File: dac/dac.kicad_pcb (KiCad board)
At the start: 4 copper layers, 50 x 25 mm, 33 parts, among them J1 USB_B, J2 Conn_01x04_Pin, J3 Conn_01x04_Pin, U1 PCM2902, U2 SPX3819M5-L, Y1 12MHz

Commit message: started layout
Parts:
- moved C3 0.50 mm to (108.7, 89.9)
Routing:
- net /CONN_D+: track 0.00 -> 21.4 mm
- net /CONN_D-: track 0.00 -> 20.6 mm
- net GND: track 0.00 -> 9.49 mm
- net /XTO: track 0.00 -> 9.29 mm
- net /VINL: track 0.00 -> 7.37 mm
- net /XTI: track 0.00 -> 6.44 mm
- net 3V7: track 0.00 -> 6.28 mm
- net VUSB_CONN: track 0.00 -> 3.87 mm
- net VDDI: track 0.00 -> 2.75 mm
- net /VINR: track 0.00 -> 2.74 mm
- net /VCCXI: track 0.00 -> 2.29 mm
- net /VCCP2I: track 0.00 -> 2.13 mm
- net /USB_D+: track 0.00 -> 2.00 mm
- net /USB_D-: track 0.00 -> 1.85 mm
- net /VCOM: track 0.00 -> 0.63 mm, vias 0 -> 1
- added copper zone on F.Cu, net GND
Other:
- board text added: "teardrop here."

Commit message: layout is complete
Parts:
- added TP2: TestPoint, TestPoint:TestPoint_Pad_D1.0mm, F.Cu at (85.8, 94.3)
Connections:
- J2 pad 1: unconnected-(J2-Pin_1-Pad1) -> VBUS
- J2 pad 2: unconnected-(J2-Pin_2-Pad2) -> GND
- J2 pad 3: unconnected-(J2-Pin_3-Pad3) -> /VOUTL
- J2 pad 4: unconnected-(J2-Pin_4-Pad4) -> /VOUTR
- J3 pad 1: unconnected-(J3-Pin_1-Pad1) -> /HID0
- J3 pad 2: unconnected-(J3-Pin_2-Pad2) -> /HID1
- J3 pad 3: unconnected-(J3-Pin_3-Pad3) -> /HID2
- J3 pad 4: unconnected-(J3-Pin_4-Pad4) -> /~{SSPND}
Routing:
- net VBUS: track 0.00 -> 43.4 mm, vias 0 -> 2
- net GND: track 9.49 -> 33.1 mm, vias 0 -> 18
- net CGND: track 0.00 -> 17.7 mm
- net VDDI: track 2.75 -> 19.6 mm
- net /HID2: track 0.00 -> 12.9 mm, vias 0 -> 1
- net /HID1: track 0.00 -> 11.9 mm, vias 0 -> 1
- net /HID0: track 0.00 -> 11.3 mm, vias 0 -> 1
- net /VOUTL: track 0.00 -> 6.56 mm
- net 3V7: track 6.28 -> 0.00 mm
- net /~{SSPND}: track 0.00 -> 5.14 mm
- net /ADJ: track 0.00 -> 4.59 mm
- net /VOUTR: track 0.00 -> 4.36 mm
- net /VCCP1I: track 0.00 -> 3.30 mm, vias 0 -> 1
- net /VCOM: track 0.63 -> 2.12 mm
- net /CONN_D+: track 21.4 -> 22.5 mm
- added copper zone on F.Cu, net 3V7
- added copper zone on In1.Cu, net GND
- added copper zone on In2.Cu, net GND
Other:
- board text removed: "teardrop here."

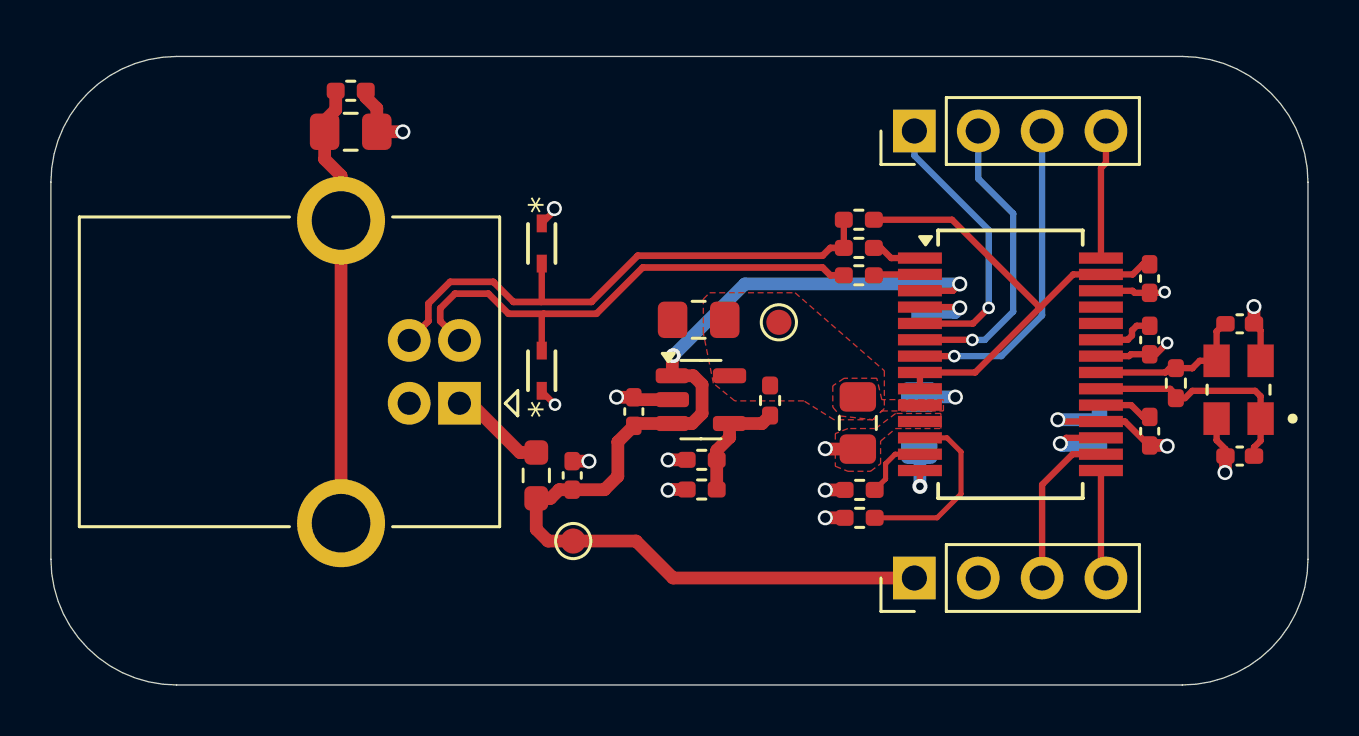
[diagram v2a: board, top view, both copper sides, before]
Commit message: added stitching, redid 3d models
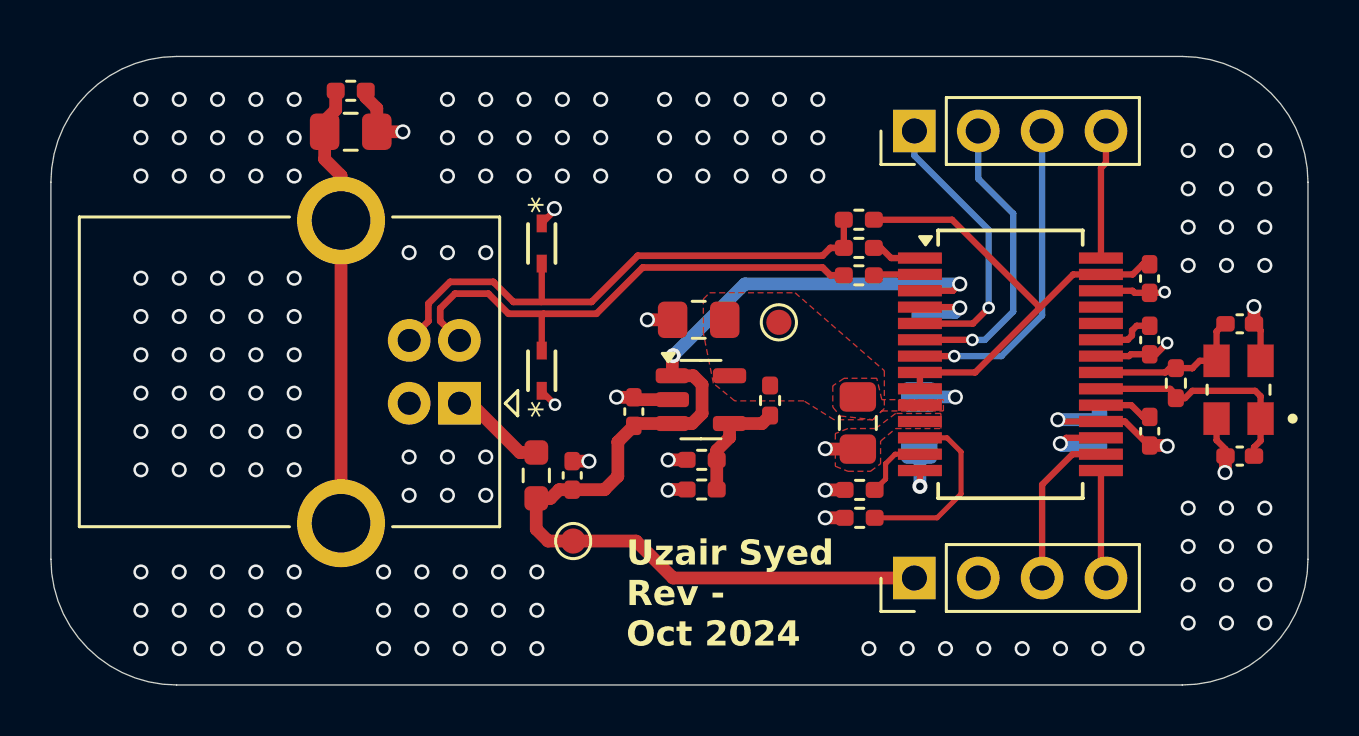
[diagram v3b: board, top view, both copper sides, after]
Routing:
- net GND: track 33.1 -> 34.1 mm, vias 18 -> 165
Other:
- board text added: "Uzair Syed Rev - Oct 2024"

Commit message: added teardrops & extra stitching
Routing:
- net GND: vias 165 -> 170
- added copper zone on F.Cu, net VDDI

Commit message: labeled headers and test points
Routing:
- net GND: vias 170 -> 159
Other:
- board text added: "3V7"
- board text added: "GND"
- board text added: "HID0"
- board text added: "HID1"
- board text added: "HID2"
- board text added: "VBUS"
- board text added: "VL"
- board text added: "VR"
- board text added: "~{SSPND}"

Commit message: final cleanup
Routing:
- net GND: vias 159 -> 161
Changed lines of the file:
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@@
 				(color "White")
 			)
-			(copper_finish "HAL SnPb")
+			(copper_finish "None")
 			(dielectric_constraints yes)
 		)
@@
 	)
 	(gr_text "GND\n"
-		(at 100.6348 98.7044 0)
+		(at 100.7364 98.7044 0)
 		(layer "F.SilkS")
 		(effects
@@
 	)
 	(gr_text "VBUS\n"
-		(at 97.5868 98.806 0)
+		(at 97.4852 98.7044 0)
 		(layer "F.SilkS")
 		(effects
@@
 	)
 	(via
+		(at 103.9876 90.9828)
+		(size 0.6)
+		(drill 0.3)
+		(layers "F.Cu" "B.Cu")
+		(free yes)
+		(net 2)
+	)
+	(via
 		(at 70.104 98.552)
 		(size 0.6)
@@
 	)
 	(via
+		(at 103.886 89.916)
+		(size 0.6)
+		(drill 0.3)
+		(layers "F.Cu" "B.Cu")
+		(free yes)
+		(net 2)
+	)
+	(via
 		(at 68.58 97.028)
 		(size 0.6)
@@
 	)
 	(zone
-		(net 8)
-		(net_name "VBUS")
+		(net 23)
+		(net_name "/VINR")
 		(layer "F.Cu")
 		(name "$teardrop_padvia$")
 		(hatch full 0.1)
-		(priority 30000)
+		(priority 30007)
 		(attr
 			(teardrop
@@
 		(polygon
 			(pts
-				(xy 97.645 95.491) (xy 97.645 95.999) (xy 98.495 96.595) (xy 99.346 95.745) (xy 98.495 94.895)
+				(xy 98.426841 90.829475) (xy 98.570525 90.973159) (xy 98.69 91.045) (xy 99.565707 90.819293) (xy 98.69 90.660946)
 			)
 		)
@@
 	)
 	(zone
-		(net 20)
-		(net_name "/VOUTL")
+		(net 1)
+		(net_name "/VCOM")
 		(layer "F.Cu")
 		(name "$teardrop_padvia$")
 		(hatch full 0.1)
-		(priority 30001)
+		(priority 30008)
 		(attr
 			(teardrop
@@
 		(polygon
 			(pts
-				(xy 104.552 94.045) (xy 104.298 94.045) (xy 103.639702 95.419719) (xy 104.425 95.746) (xy 105.210298 95.419719)
+				(xy 99.438 91.92) (xy 99.692 91.92) (xy 99.79 91.695) (xy 99.565 91.469) (xy 99.34 91.695)
 			)
 		)
 	)
 	(zone
-		(net 24)
-		(net_name "/VINL")
+		(net 20)
+		(net_name "/VOUTL")
 		(layer "F.Cu")
 		(name "$teardrop_padvia$")
 		(hatch full 0.1)
-		(priority 30005)
+		(priority 30001)
 		(attr
 			(teardrop
@@
 		(polygon
 			(pts
-				(xy 98.443 93.4526) (xy 98.443 93.2494) (xy 98.024229 93.043179) (xy 97.7645 93.351) (xy 98.024229 93.658821)
+				(xy 104.552 94.045) (xy 104.298 94.045) (xy 103.639702 95.419719) (xy 104.425 95.746) (xy 105.210298 95.419719)
 			)
 		)
 	)
 	(zone
-		(net 18)
-		(net_name "/VOUTR")
+		(net 20)
+		(net_name "/VOUTL")
 		(layer "F.Cu")
 		(name "$teardrop_padvia$")
 		(hatch full 0.1)
-		(priority 30009)
+		(priority 30003)
 		(attr
 			(teardrop
@@
 		(polygon
 			(pts
-				(xy 106.638 91.92) (xy 106.892 91.92) (xy 106.99 91.695) (xy 106.765 91.469) (xy 106.54 91.695)
-			)
-		)
-	)
-	(zone
-		(net 7)
-		(net_name "3V7")
-		(layer "F.Cu")
-		(hatch edge 0.5)
-		(priority 1)
-		(connect_pads yes
-			(clearance 0.2032)
-		)
-		(min_thickness 0.25)
-		(filled_areas_thickness no)
-		(fill yes
-			(thermal_gap 0.5)
-			(thermal_bridge_width 0.5)
-		)
-		(polygon
-			(pts
-				(xy 90.95 86) (xy 90.95 84.65) (xy 91.2 84.4) (xy 94.6 84.4) (xy 98.15 87.5) (xy 98.15 89) (xy 97.7 89.45)
-				(xy 96.15 89.45) (xy 94.95 88.7) (xy 92.2 88.7) (xy 91.35 88)
+				(xy 105.665 90.693) (xy 105.665 90.947) (xy 105.89 91.045) (xy 106.766 90.82) (xy 105.89 90.595)
 			)
 		)
 	)
 	(zone
-		(net 18)
-		(net_name "/VOUTR")
+		(net 8)
+		(net_name "VBUS")
 		(layer "F.Cu")
 		(name "$teardrop_padvia$")
 		(hatch full 0.1)
-		(priority 30002)
+		(priority 30000)
 		(attr
 			(teardrop
@@
 		(polygon
 			(pts
-				(xy 106.892 94.084782) (xy 106.638 94.084782) (xy 106.179702 95.419719) (xy 106.965 95.746) (xy 107.750298 95.419719)
+				(xy 97.645 95.491) (xy 97.645 95.999) (xy 98.495 96.595) (xy 99.346 95.745) (xy 98.495 94.895)
 			)
 		)
 	)
 	(zone
-		(net 1)
-		(net_name "/VCOM")
+		(net 24)
+		(net_name "/VINL")
 		(layer "F.Cu")
 		(name "$teardrop_padvia$")
 		(hatch full 0.1)
-		(priority 30008)
+		(priority 30005)
 		(attr
 			(teardrop
@@
 		(polygon
 			(pts
-				(xy 99.438 91.92) (xy 99.692 91.92) (xy 99.79 91.695) (xy 99.565 91.469) (xy 99.34 91.695)
+				(xy 98.443 93.4526) (xy 98.443 93.2494) (xy 98.024229 93.043179) (xy 97.7645 93.351) (xy 98.024229 93.658821)
 			)
 		)
 	)
 	(zone
-		(net 2)
-		(net_name "GND")
+		(net 7)
+		(net_name "3V7")
 		(layer "F.Cu")
 		(hatch edge 0.5)
+		(priority 1)
 		(connect_pads yes
 			(clearance 0.2032)
@@
 		(polygon
 			(pts
-				(xy 100.4 89.8) (xy 100.4 89.2) (xy 98.6 89.2) (xy 97.8 89.8) (xy 96.7 89.8) (xy 96.2 90) (xy 96.2 91.3)
-				(xy 96.7 91.5) (xy 97.6 91.5) (xy 98 91.2) (xy 98 90.3) (xy 98.6 89.8)
+				(xy 90.7976 86.0508) (xy 90.7976 84.7008) (xy 91.2 84.4) (xy 94.6 84.4) (xy 98.15 87.5) (xy 98.15 89)
+				(xy 97.7 89.45) (xy 96.15 89.45) (xy 94.95 88.7) (xy 90.855 88.65) (xy 90.8812 88.0364)
 			)
 		)
 	)
 	(zone
-		(net 20)
-		(net_name "/VOUTL")
+		(net 24)
+		(net_name "/VINL")
 		(layer "F.Cu")
 		(name "$teardrop_padvia$")
 		(hatch full 0.1)
-		(priority 30003)
+		(priority 30004)
 		(attr
 			(teardrop
@@
 		(polygon
 			(pts
-				(xy 105.665 90.693) (xy 105.665 90.947) (xy 105.89 91.045) (xy 106.766 90.82) (xy 105.89 90.595)
+				(xy 100.586773 90.257256) (xy 100.730456 90.113573) (xy 100.44 89.957169) (xy 99.564293 90.169293)
+				(xy 100.44 90.395)
 			)
 		)
 	)
 	(zone
-		(net 6)
-		(net_name "VDDI")
+		(net 18)
+		(net_name "/VOUTR")
 		(layer "F.Cu")
-		(hatch edge 0.5)
-		(priority 4)
+		(name "$teardrop_padvia$")
+		(hatch full 0.1)
+		(priority 30009)
+		(attr
+			(teardrop
+				(type padvia)
+			)
+		)
 		(connect_pads yes
-			(clearance 0.2032)
+			(clearance 0)
 		)
-		(min_thickness 0.25)
+		(min_thickness 0.0254)
 		(filled_areas_thickness no)
 		(fill yes
@@
 		(polygon
 			(pts
-				(xy 98.7044 88.4428) (xy 100.4316 88.4428) (xy 100.44 87.345) (xy 98.6028 87.3252)
+				(xy 106.638 91.92) (xy 106.892 91.92) (xy 106.99 91.695) (xy 106.765 91.469) (xy 106.54 91.695)
 			)
 		)
 	)
 	(zone
-		(net 23)
-		(net_name "/VINR")
+		(net 18)
+		(net_name "/VOUTR")
 		(layer "F.Cu")
 		(name "$teardrop_padvia$")
 		(hatch full 0.1)
-		(priority 30007)
+		(priority 30002)
 		(attr
 			(teardrop
@@
 		(polygon
 			(pts
-				(xy 98.426841 90.829475) (xy 98.570525 90.973159) (xy 98.69 91.045) (xy 99.565707 90.819293) (xy 98.69 90.660946)
+				(xy 106.892 94.084782) (xy 106.638 94.084782) (xy 106.179702 95.419719) (xy 106.965 95.746) (xy 107.750298 95.419719)
 			)
 		)
 	)
 	(zone
-		(net 24)
-		(net_name "/VINL")
+		(net 2)
+		(net_name "GND")
 		(layer "F.Cu")
-		(name "$teardrop_padvia$")
-		(hatch full 0.1)
-		(priority 30004)
-		(attr
-			(teardrop
-				(type padvia)
+		(hatch edge 0.5)
+		(connect_pads yes
+			(clearance 0.2032)
+		)
+		(min_thickness 0.25)
+		(filled_areas_thickness no)
+		(fill yes
+			(thermal_gap 0.5)
+			(thermal_bridge_width 0.5)
+		)
+		(polygon
+			(pts
+				(xy 100.4 89.8) (xy 100.4 89.2) (xy 98.6 89.2) (xy 97.8 89.8) (xy 96.7 89.8) (xy 96.2 90) (xy 96.2 91.3)
+				(xy 96.7 91.5) (xy 97.6 91.5) (xy 98 91.2) (xy 98 90.3) (xy 98.6 89.8)
 			)
 		)
+	)
+	(zone
+		(net 6)
+		(net_name "VDDI")
+		(layer "F.Cu")
+		(hatch edge 0.5)
+		(priority 4)
 		(connect_pads yes
-			(clearance 0)
+			(clearance 0.2032)
 		)
-		(min_thickness 0.0254)
+		(min_thickness 0.25)
 		(filled_areas_thickness no)
 		(fill yes
@@
 		(polygon
 			(pts
-				(xy 100.586773 90.257256) (xy 100.730456 90.113573) (xy 100.44 89.957169) (xy 99.564293 90.169293)
-				(xy 100.44 90.395)
+				(xy 98.7044 88.4428) (xy 100.4316 88.4428) (xy 100.44 87.345) (xy 98.6028 87.3252)
 			)
 		)
